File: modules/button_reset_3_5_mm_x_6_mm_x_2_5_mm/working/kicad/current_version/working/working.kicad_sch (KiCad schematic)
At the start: 1 part, among them J2 b3560s

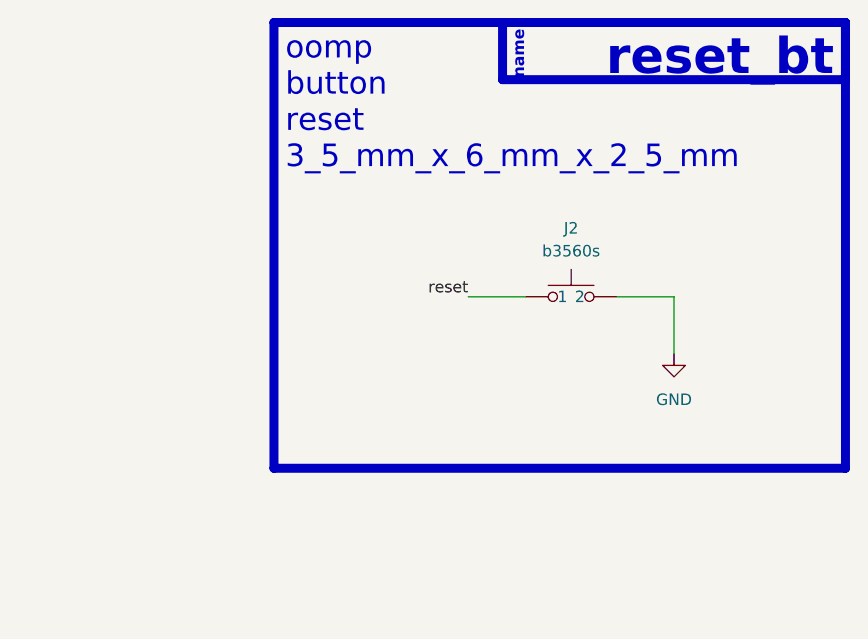
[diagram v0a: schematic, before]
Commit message: fixed formatting to be more consistent
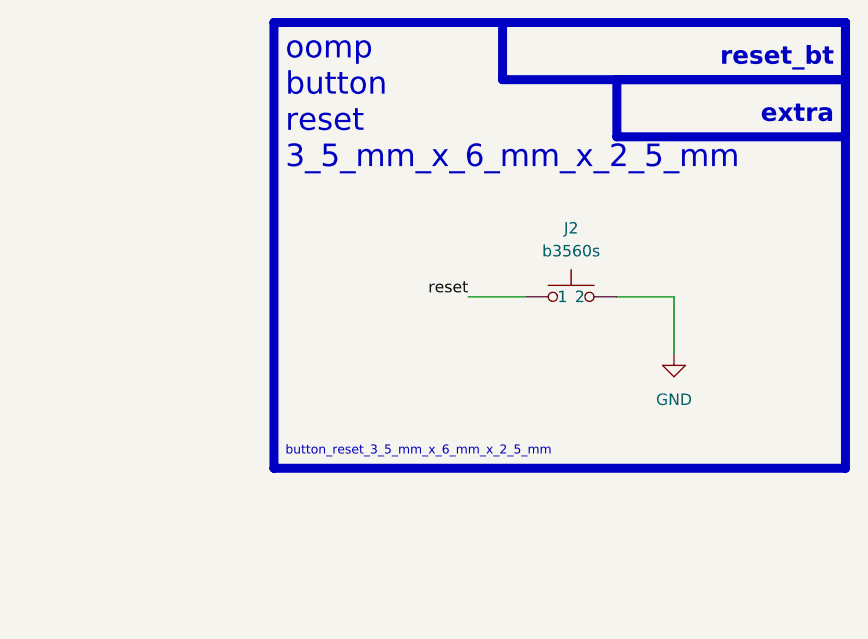
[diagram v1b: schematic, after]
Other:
- note added: "button_reset_3_5_mm_x_6_mm_x_2_5_mm"
- note added: "extra"
- note removed: "name"
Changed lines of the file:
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@@
+    (fill (type none))
+  )
+  (rectangle (start 139.7 26.67) (end 165.1 33.02)
+    (stroke (width 1) (type default))
     (fill (type none))
   )
@@
   (rectangle (start 127 20.32) (end 165.1 26.67)
     (stroke (width 1) (type default))
-    (fill (type color) (color 0 0 0 0))
+    (fill (type none))
+  )
+  (text "extra" (at 163.83 31.75 0)
+    (effects (font (size 2 2) (thickness 0.8) bold) (justify right bottom))
   )
   (text "oomp\nbutton\nreset\n3_5_mm_x_6_mm_x_2_5_mm\n" (at 102.87 36.83 0)
     (effects (font (size 2.5 2.5)) (justify left bottom))
   )
-  (text "name" (at 129.54 26.67 90)
-    (effects (font (size 1.27 1.27) (thickness 0.254) bold (color 255 255 255 1)) (justify left bottom))
+  (text "button_reset_3_5_mm_x_6_mm_x_2_5_mm" (at 102.87 68.58 0)
+    (effects (font (size 1 1)) (justify left bottom))
   )
-  (text "reset_bt\n" (at 163.83 26.67 0)
-    (effects (font (size 4 4) (thickness 0.8) bold (color 255 255 255 1)) (justify right bottom))
+  (text "reset_bt\n" (at 163.83 25.4 0)
+    (effects (font (size 2 2) (thickness 0.8) bold) (justify right bottom))
   )
   (label "reset" (at 123.19 50.8 180) (fields_autoplaced)

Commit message: schematic formatting
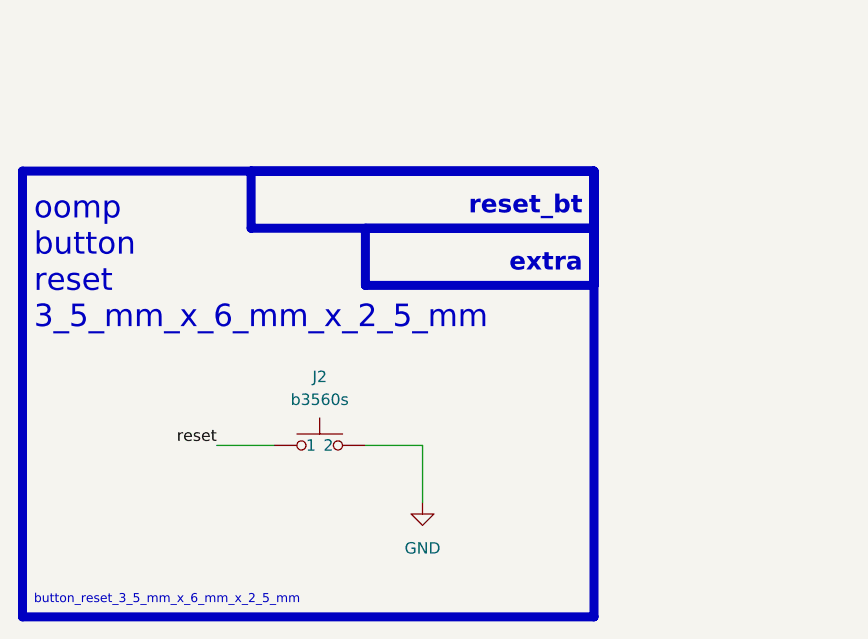
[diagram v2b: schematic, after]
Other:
- moved on the sheet: J2
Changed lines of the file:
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@@
 (kicad_sch (version 20230121) (generator eeschema)
-  (paper "A4")
-  (wire (pts (xy 123.19 50.8) (xy 129.54 50.8))
+  (paper "A5")
+  (wire (pts (xy 95.25 67.31) (xy 101.6 67.31))
     (stroke (width 0) (type default))
   )
-  (wire (pts (xy 146.05 50.8) (xy 139.7 50.8))
+  (wire (pts (xy 118.11 67.31) (xy 111.76 67.31))
     (stroke (width 0) (type default))
   )
-  (wire (pts (xy 146.05 57.15) (xy 146.05 50.8))
+  (wire (pts (xy 118.11 73.66) (xy 118.11 67.31))
     (stroke (width 0) (type default))
   )
-  (rectangle (start 166.37 83.82) (end 166.37 83.82)
+  (rectangle (start 138.43 100.33) (end 138.43 100.33)
     (stroke (width 0) (type default))
     (fill (type none))
   )
-  (rectangle (start 139.7 26.67) (end 165.1 33.02)
+  (rectangle (start 111.76 43.18) (end 137.16 49.53)
     (stroke (width 1) (type default))
     (fill (type none))
   )
-  (rectangle (start 101.6 20.32) (end 165.1 69.85)
+  (rectangle (start 73.66 36.83) (end 137.16 86.36)
     (stroke (width 1) (type default))
     (fill (type none))
   )
-  (rectangle (start 127 20.32) (end 165.1 26.67)
+  (rectangle (start 99.06 36.83) (end 137.16 43.18)
     (stroke (width 1) (type default))
     (fill (type none))
   )
-  (text "extra" (at 163.83 31.75 0)
+  (text "extra" (at 135.89 48.26 0)
     (effects (font (size 2 2) (thickness 0.8) bold) (justify right bottom))
   )
-  (text "oomp\nbutton\nreset\n3_5_mm_x_6_mm_x_2_5_mm\n" (at 102.87 36.83 0)
+  (text "oomp\nbutton\nreset\n3_5_mm_x_6_mm_x_2_5_mm\n" (at 74.93 54.61 0)
     (effects (font (size 2.5 2.5)) (justify left bottom))
   )
-  (text "button_reset_3_5_mm_x_6_mm_x_2_5_mm" (at 102.87 68.58 0)
+  (text "button_reset_3_5_mm_x_6_mm_x_2_5_mm" (at 74.93 85.09 0)
     (effects (font (size 1 1)) (justify left bottom))
   )
-  (text "reset_bt\n" (at 163.83 25.4 0)
+  (text "reset_bt\n" (at 135.89 41.91 0)
     (effects (font (size 2 2) (thickness 0.8) bold) (justify right bottom))
   )
-  (label "reset" (at 123.19 50.8 180) (fields_autoplaced)
+  (label "reset" (at 95.25 67.31 180) (fields_autoplaced)
     (effects (font (size 1.27 1.27)) (justify right bottom))
   )
-  (symbol (lib_id "oomlout_oomp_part_symbols:b3560s_electronic_button_3_5_mm_x_6_mm_x_2_5_mm_surface_mount") (at 134.62 50.8 0) (unit 1)
+  (symbol (lib_id "oomlout_oomp_part_symbols:b3560s_electronic_button_3_5_mm_x_6_mm_x_2_5_mm_surface_mount") (at 106.68 67.31 0) (unit 1)
     (in_bom yes) (on_board yes) (dnp no) (fields_autoplaced)
-    (property "Reference" "J2" (at 134.62 43.18 0)
+    (property "Reference" "J2" (at 106.68 59.69 0)
       (effects (font (size 1.27 1.27)))
     )
-    (property "Value" "b3560s" (at 134.62 45.72 0)
+    (property "Value" "b3560s" (at 106.68 62.23 0)
       (effects (font (size 1.27 1.27)))
     )
-    (property "Footprint" "b3560s_electronic_button_3_5_mm_x_6_mm_x_2_5_mm_surface_mount" (at 134.62 45.72 0)
+    (property "Footprint" "b3560s_electronic_button_3_5_mm_x_6_mm_x_2_5_mm_surface_mount" (at 106.68 62.23 0)
       (effects (font (size 1.27 1.27)) hide)
     )
-    (property "Datasheet" "https://github.com/oomlout/oomlout_oomp_v3/parts/electronic_button_3_5_mm_x_6_mm_x_2_5_mm_surface_mount/datasheet.pdf" (at 134.62 45.72 0)
+    (property "Datasheet" "https://github.com/oomlout/oomlout_oomp_v3/parts/electronic_button_3_5_mm_x_6_mm_x_2_5_mm_surface_mount/datasheet.pdf" (at 106.68 62.23 0)
       (effects (font (size 1.27 1.27)) hide)
     )
@@
     )
   )
-  (symbol (lib_id "power:GND") (at 146.05 57.15 0) (unit 1)
+  (symbol (lib_id "power:GND") (at 118.11 73.66 0) (unit 1)
     (in_bom yes) (on_board yes) (dnp no) (fields_autoplaced)
-    (property "Reference" "#PWR04" (at 146.05 63.5 0)
+    (property "Reference" "#PWR04" (at 118.11 80.01 0)
       (effects (font (size 1.27 1.27)) hide)
     )
-    (property "Value" "GND" (at 146.05 62.23 0)
+    (property "Value" "GND" (at 118.11 78.74 0)
       (effects (font (size 1.27 1.27)))
     )
-    (property "Footprint" "" (at 146.05 57.15 0)
+    (property "Footprint" "" (at 118.11 73.66 0)
       (effects (font (size 1.27 1.27)) hide)
     )
-    (property "Datasheet" "" (at 146.05 57.15 0)
+    (property "Datasheet" "" (at 118.11 73.66 0)
       (effects (font (size 1.27 1.27)) hide)
     )
